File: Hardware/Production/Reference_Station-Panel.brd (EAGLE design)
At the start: 152.4 x 101.6 mm, 395 parts, among them J10 ANTENNA-SMA-GROUNDEDEDGE_SMA, J11 Vertical Qwiic Connector, J2 ANTENNA-SMA-GROUNDEDEDGE_SMA, J3 MICRO-SD-PUSH-PUSH-EXT-PIN, J4 Vertical Qwiic Connector, J7 ANTENNA-SMA-GROUNDEDEDGE_RPSMA, J9 MAGJACK-POE, U1 ESP-WROOM-32E, U10 POE_PSU-DP990X, U11 OPA344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

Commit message: v10 Hardware
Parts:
- removed FRAME1: FRAME-LEDGER, SparkFun-Aesthetics:CREATIVE_COMMONS
- removed LOGO1: SPECIAL_INSTRUCTIONS-ORDERING, SparkFun-Aesthetics:ORDERING_INSTRUCTIONS
- removed VPOE7: TEST-POINTPOGO_PTH, SparkFun-Connectors:1X01_NO_SILK
- added C58: 0.1uF, SparkFun-Capacitors:0603
- added DET, GND: TEST-POINTPOGO_PTH, SparkFun-Connectors:1X01_NO_SILK
- added E$1, E$2, E$3, E$4: (no value), SparkFun-Aesthetics:FIDUCIAL-1X2
- added E$5, E$6: (no value), SparkFun-Retired:FIDUCIAL-1.5X3
- added GNSS_RESET: JUMPER-COMBO_2_NO, SparkFun-Jumpers:COMBO-JUMPER_2_NO
- added R64: 10k, SparkFun-Resistors:0603
- added R65: 100k, SparkFun-Resistors:0603
- added U$154: (no value), output:#GNSS_RESET#0
- added U$155, U$156: (no value), output:DET0
- C31: value DNP -> 0.1uF; device SparkFun-Capacitors:0603_NO_CREAM -> SparkFun-Capacitors:0603
- U$70: device output:CORS_AND_TIME0 -> output:#GNSS_#RESET##0
- U$74: device output:CORS_AND_TIME0 -> output:#RESET#0
- U8: value ADC8045 -> MCP6021T; device SparkFun-IC-Amplifiers:SO08_PAD -> SparkFun-IC-Amplifiers:SOT23-5
- U9: value 74HC4066_QUAD_BILATERAL_SWITCH_QFN -> 74LVC4066D_QUAD_BILATERAL_SWITCH; device SparkFun-IC-Logic:14-QFN -> SparkFun-IC-Logic:SO14
- moved U$74 48.4 mm to (112.7, 61.0), flipped to the top
- moved U$70 35.6 mm to (117.8, 62.9), flipped to the bottom
- moved U$22 10.5 mm to (112.1, 99.4)
- moved U$21 10.5 mm to (89.9, 101.1)
- moved C23 9.93 mm to (120.3, 86.7), turned to 270 degrees
- moved C22 8.98 mm to (120.3, 91.1), turned to 90 degrees
- moved U$41 5.44 mm to (147.5, 61.0)
- moved C26 3.20 mm to (37.1, 32.4)
- moved U9 3.02 mm to (35.2, 26.7), turned to 270 degrees
- moved U$152 2.56 mm to (129.2, 22.9)
- moved U$75 2.56 mm to (75.9, 29.2)
- moved U$153 2.56 mm to (75.9, 22.9)
- moved U$73 2.56 mm to (129.2, 29.2)
- moved R23 2.54 mm to (115.6, 85.1), turned to 0 degrees
- moved R44 2.54 mm to (114.4, 82.5)
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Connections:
- removed net N$16: R9.2, U8.6
- new net DET: DET.1, J3.9, R65.1, U1.4
- new net GNSS_!RESET!: C58.1, GNSS_RESET.1, GNSS_RESET.3, R64.1, U4.49
- net !RESET!: now also GNSS_RESET.2, GNSS_RESET.4; no longer U4.49
- net 3.3V: now also R64.2
- net 3.3V_SW: now also R65.2
- net 5V: now also U8.5; no longer U8.7
- net GND: now also C58.2, GND.1, U8.2; no longer U8.4, U8.PAD, U9.EPAD, VPOE7.1
- net N$18: now also U8.4; no longer U8.2
- net N$26: now also R9.2
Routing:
- net DET: track 0.00 -> 118.1 mm, vias 0 -> 4
- net GNSS_!RESET!: track 0.00 -> 35.8 mm, vias 0 -> 1
- net !RESET!: track 256.6 -> 226.9 mm, vias 9 -> 8
- net ESP25/TP: track 101.6 -> 113.9 mm
- net N$26: track 7.10 -> 13.9 mm, vias 1 -> 2
- net 5V: track 225.2 -> 219.4 mm, vias 43 -> 45
- net ESP2/DAT0: track 89.6 -> 94.2 mm
- net SD_CMD: track 17.4 -> 21.2 mm
- net SD_DAT2: track 23.4 -> 27.0 mm
- net PWREN: track 89.6 -> 93.1 mm, vias 4 -> 2
- net 3.3V_SW: track 348.0 -> 351.3 mm
- net N$16: track 2.96 -> 0.00 mm
- net ESP15/CMD: track 88.8 -> 91.3 mm
- net SD_DAT0: track 25.5 -> 27.8 mm
- net N$29: track 3.71 -> 5.49 mm
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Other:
- board size 152.4 x 101.6 mm -> 165.5 x 131.1 mm
- board text added: "Route Out"
- board text added: "v-score"
- board text added: "v10"
- board text removed: "4-Layers 1.6mm Thickness 1oz Copper Lead-Free HASL Finish Red Solder Resist White Silkscreen"
- board text removed: "Dimensions In Inches"
- board text removed: "Paul Clark"
- board text removed: "v01"

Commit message: Improve TP output at 5V
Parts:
- added R66: 100k, SparkFun-Resistors:0603
- moved Y1 3.56 mm to (62.2, 76.1)
- moved C27 2.69 mm to (66.9, 77.1)
- moved C28 2.69 mm to (66.9, 75.3)
- moved R44 1.63 mm to (115.4, 81.3)
- moved R24 1.52 mm to (64.3, 76.2)
- moved R23 1.37 mm to (116.1, 83.8)
- moved U$71 1.30 mm to (115.4, 82.2)
- moved V_TP 1.30 mm to (115.4, 81.3)
- moved R18 1.28 mm to (117.0, 81.3)
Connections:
- net N$18: now also R66.2
- net N$26: now also R66.1
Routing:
- net N$26: track 13.9 -> 18.1 mm
- net N$20: track 12.2 -> 8.16 mm
- net ESP25/TP: track 113.9 -> 117.5 mm
- net N$19: track 11.6 -> 8.96 mm
- net ESP22/SCL: track 171.6 -> 170.0 mm
- net ESP21/SDA: track 180.3 -> 179.0 mm
- net GND: vias 327 -> 326

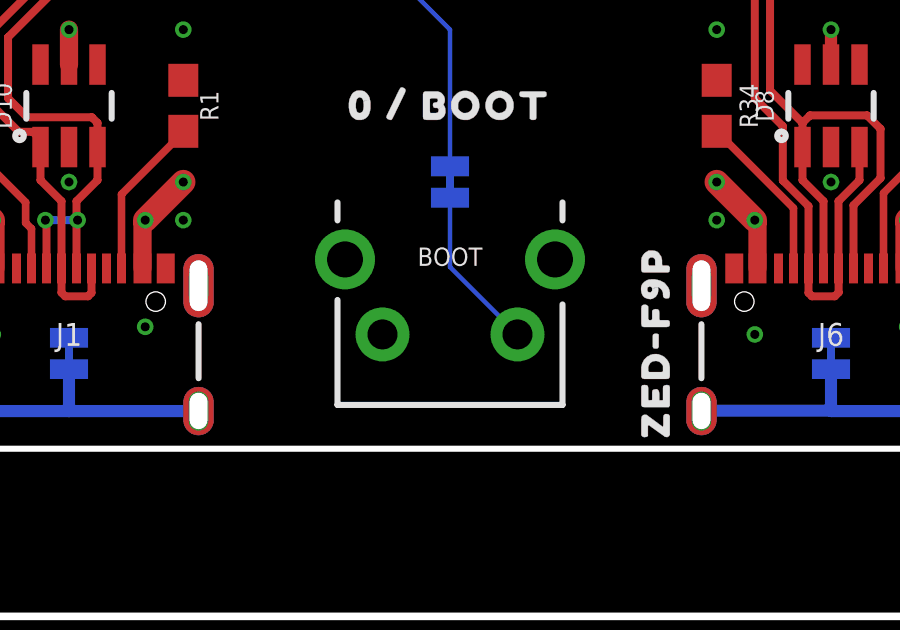
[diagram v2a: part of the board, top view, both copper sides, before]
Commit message: Move BOOT / MODE button further out. Update panels and stickers
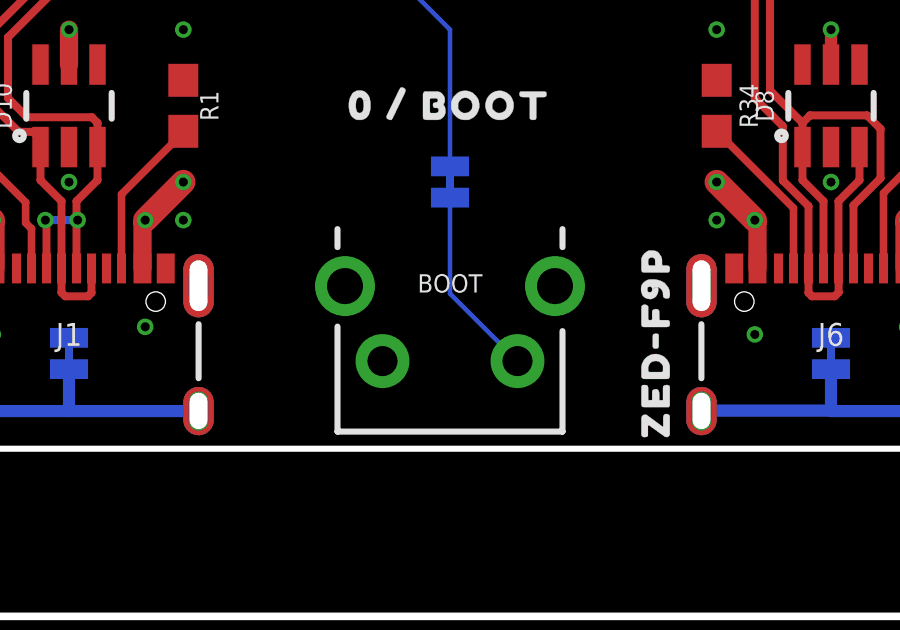
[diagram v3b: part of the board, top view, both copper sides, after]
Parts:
- moved BOOT 0.89 mm to (126.7, 2.92)
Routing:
- net N$29: track 5.49 -> 6.38 mm
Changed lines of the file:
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@@
 <layers>
 <layer number="1" name="Top" color="4" fill="1" visible="yes" active="yes"/>
-<layer number="2" name="Route2" color="16" fill="1" visible="no" active="yes"/>
+<layer number="2" name="Route2" color="63" fill="1" visible="no" active="yes"/>
 <layer number="3" name="Route3" color="17" fill="1" visible="no" active="no"/>
 <layer number="4" name="Route4" color="18" fill="1" visible="no" active="no"/>
@@
 <layer number="19" name="Unrouted" color="6" fill="1" visible="yes" active="yes"/>
 <layer number="20" name="Dimension" color="24" fill="1" visible="yes" active="yes"/>
-<layer number="21" name="tPlace" color="7" fill="1" visible="yes" active="yes"/>
-<layer number="22" name="bPlace" color="7" fill="1" visible="yes" active="yes"/>
+<layer number="21" name="tPlace" color="16" fill="1" visible="yes" active="yes"/>
+<layer number="22" name="bPlace" color="14" fill="1" visible="yes" active="yes"/>
 <layer number="23" name="tOrigins" color="15" fill="1" visible="yes" active="yes"/>
 <layer number="24" name="bOrigins" color="15" fill="1" visible="yes" active="yes"/>
-<layer number="25" name="tNames" color="7" fill="1" visible="yes" active="yes"/>
-<layer number="26" name="bNames" color="7" fill="1" visible="yes" active="yes"/>
-<layer number="27" name="tValues" color="7" fill="1" visible="yes" active="yes"/>
-<layer number="28" name="bValues" color="7" fill="1" visible="yes" active="yes"/>
-<layer number="29" name="tStop" color="7" fill="3" visible="yes" active="yes"/>
-<layer number="30" name="bStop" color="7" fill="6" visible="yes" active="yes"/>
-<layer number="31" name="tCream" color="7" fill="4" visible="yes" active="yes"/>
-<layer number="32" name="bCream" color="7" fill="5" visible="yes" active="yes"/>
-<layer number="33" name="tFinish" color="6" fill="3" visible="yes" active="yes"/>
-<layer number="34" name="bFinish" color="6" fill="6" visible="yes" active="yes"/>
-<layer number="35" name="tGlue" color="7" fill="4" visible="yes" active="yes"/>
-<layer number="36" name="bGlue" color="7" fill="5" visible="yes" active="yes"/>
-<layer number="37" name="tTest" color="7" fill="1" visible="yes" active="yes"/>
-<layer number="38" name="bTest" color="7" fill="1" visible="yes" active="yes"/>
-<layer number="39" name="tKeepout" color="4" fill="11" visible="yes" active="yes"/>
-<layer number="40" name="bKeepout" color="1" fill="11" visible="yes" active="yes"/>
-<layer number="41" name="tRestrict" color="4" fill="10" visible="yes" active="yes"/>
-<layer number="42" name="bRestrict" color="1" fill="10" visible="yes" active="yes"/>
-<layer number="43" name="vRestrict" color="2" fill="10" visible="yes" active="yes"/>
-<layer number="44" name="Drills" color="7" fill="1" visible="yes" active="yes"/>
+<layer number="25" name="tNames" color="7" fill="1" visible="no" active="yes"/>
+<layer number="26" name="bNames" color="7" fill="1" visible="no" active="yes"/>
+<layer number="27" name="tValues" color="7" fill="1" visible="no" active="yes"/>
+<layer number="28" name="bValues" color="7" fill="1" visible="no" active="yes"/>
+<layer number="29" name="tStop" color="7" fill="3" visible="no" active="yes"/>
+<layer number="30" name="bStop" color="7" fill="6" visible="no" active="yes"/>
+<layer number="31" name="tCream" color="7" fill="4" visible="no" active="yes"/>
+<layer number="32" name="bCream" color="7" fill="5" visible="no" active="yes"/>
+<layer number="33" name="tFinish" color="6" fill="3" visible="no" active="yes"/>
+<layer number="34" name="bFinish" color="6" fill="6" visible="no" active="yes"/>
+<layer number="35" name="tGlue" color="7" fill="4" visible="no" active="yes"/>
+<layer number="36" name="bGlue" color="7" fill="5" visible="no" active="yes"/>
+<layer number="37" name="tTest" color="7" fill="1" visible="no" active="yes"/>
+<layer number="38" name="bTest" color="7" fill="1" visible="no" active="yes"/>
+<layer number="39" name="tKeepout" color="4" fill="11" visible="no" active="yes"/>
+<layer number="40" name="bKeepout" color="1" fill="11" visible="no" active="yes"/>
+<layer number="41" name="tRestrict" color="4" fill="10" visible="no" active="yes"/>
+<layer number="42" name="bRestrict" color="1" fill="10" visible="no" active="yes"/>
+<layer number="43" name="vRestrict" color="2" fill="10" visible="no" active="yes"/>
+<layer number="44" name="Drills" color="7" fill="1" visible="no" active="yes"/>
 <layer number="45" name="Holes" color="7" fill="1" visible="yes" active="yes"/>
-<layer number="46" name="Milling" color="3" fill="1" visible="yes" active="yes"/>
-<layer number="47" name="Measures" color="7" fill="1" visible="yes" active="yes"/>
-<layer number="48" name="Document" color="7" fill="1" visible="yes" active="yes"/>
-<layer number="49" name="Reference" color="7" fill="1" visible="yes" active="yes"/>
-<layer number="50" name="dxf" color="7" fill="1" visible="yes" active="yes"/>
-<layer number="51" name="tDocu" color="7" fill="1" visible="yes" active="yes"/>
-<layer number="52" name="bDocu" color="7" fill="1" visible="yes" active="yes"/>
+<layer number="46" name="Milling" color="3" fill="1" visible="no" active="yes"/>
+<layer number="47" name="Measures" color="7" fill="1" visible="no" active="yes"/>
+<layer number="48" name="Document" color="7" fill="1" visible="no" active="yes"/>
+<layer number="49" name="Reference" color="7" fill="1" visible="no" active="yes"/>
+<layer number="50" name="dxf" color="7" fill="1" visible="no" active="yes"/>
+<layer number="51" name="tDocu" color="6" fill="1" visible="yes" active="yes"/>
+<layer number="52" name="bDocu" color="7" fill="1" visible="no" active="yes"/>
 <layer number="53" name="tGND_GNDA" color="7" fill="9" visible="no" active="no"/>
 <layer number="54" name="bGND_GNDA" color="1" fill="9" visible="no" active="no"/>
@@
 <attribute name="PROD_ID" value="SWCH-13896" x="101.2825" y="3.81" size="1.778" layer="27" ratio="15" display="off"/>
 </element>
-<element name="BOOT" library="SparkFun-Switches" package="TACTILE_SWITCH_PTH_RA_8-020" value="MOMENTARY-SWITCH-SPST-PTH-RIGHT-ANGLE-8-020" x="126.6825" y="3.81" smashed="yes">
-<attribute name="NAME" x="126.6825" y="6.096" size="0.6096" layer="25" font="vector" ratio="20" align="bottom-center"/>
-<attribute name="PROD_ID" value="SWCH-13896" x="126.6825" y="3.81" size="1.778" layer="27" ratio="15" display="off"/>
+<element name="BOOT" library="SparkFun-Switches" package="TACTILE_SWITCH_PTH_RA_8-020" value="MOMENTARY-SWITCH-SPST-PTH-RIGHT-ANGLE-8-020" x="126.6825" y="2.921" smashed="yes">
+<attribute name="NAME" x="126.6825" y="5.207" size="0.6096" layer="25" font="vector" ratio="20" align="bottom-center"/>
+<attribute name="PROD_ID" value="SWCH-13896" x="126.6825" y="2.921" size="1.778" layer="27" ratio="15" display="off"/>
 </element>
 <element name="LED" library="SparkFun-Jumpers" package="SMT-JUMPER_2_NC_TRACE_SILK" package3d_urn="urn:adsk.eagle:package:39281/1" value="JUMPER-SMT_2_NC_TRACE_SILK" x="12.3825" y="3.175" smashed="yes" rot="MR180">
@@
 <wire x1="117.0305" y1="79.248" x2="117.0305" y2="80.43" width="0" layer="19" extent="1-1"/>
 <wire x1="116.9425" y1="64.135" x2="125.9365" y2="63.57" width="0" layer="19" extent="1-1"/>
-<wire x1="124.4325" y1="3.81" x2="135.5725" y2="7.62" width="0" layer="19" extent="1-1"/>
-<wire x1="117.2075" y1="6.01" x2="124.4325" y2="3.81" width="0" layer="19" extent="1-1"/>
+<wire x1="124.4325" y1="2.921" x2="135.5725" y2="7.62" width="0" layer="19" extent="1-1"/>
+<wire x1="117.2075" y1="6.01" x2="124.4325" y2="2.921" width="0" layer="19" extent="1-1"/>
 <wire x1="117.7925" y1="7.62" x2="117.2075" y2="6.01" width="0" layer="19" extent="1-1"/>
 <wire x1="116.5225" y1="4.064" x2="117.2075" y2="6.01" width="0" layer="19" extent="1-1"/>
@@
 <contactref element="BOOT" pad="2"/>
 <contactref element="BOOT_SW" pad="2"/>
-<wire x1="128.9325" y1="3.81" x2="126.6825" y2="6.06" width="0.1524" layer="16"/>
-<wire x1="126.6825" y1="6.06" x2="126.6825" y2="8.3693" width="0.1524" layer="16"/>
+<wire x1="126.6825" y1="5.171" x2="128.9325" y2="2.921" width="0.1524" layer="16"/>
+<wire x1="126.6825" y1="8.3693" x2="126.6825" y2="5.171" width="0.1524" layer="16"/>
 </signal>
 <signal name="GNSS_!RESET!">

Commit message: Replace OPA344 with MCP6021T-E/OT
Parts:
- U11, U13: value OPA344 -> MCP6021T
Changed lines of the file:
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@@
 <attribute name="VALUE" x="119.0625" y="54.102" size="0.6096" layer="27" font="vector" ratio="20" rot="R180" align="top-center"/>
 </element>
-<element name="U11" library="SparkFun-IC-Amplifiers" package="SOT23-5" value="OPA344" x="128.5875" y="78.74" smashed="yes" rot="R90">
+<element name="U11" library="SparkFun-IC-Amplifiers" package="SOT23-5" value="MCP6021T" x="128.5875" y="78.74" smashed="yes" rot="R90">
 <attribute name="NAME" x="128.5875" y="76.835" size="0.6096" layer="25" font="vector" ratio="20" rot="R180" align="bottom-center"/>
-<attribute name="PROD_ID" value="IC-08251" x="124.7775" y="74.93" size="1.778" layer="27" ratio="15" rot="R90" display="off"/>
+<attribute name="PROD_ID" value="IC-12504" x="124.7775" y="74.93" size="1.778" layer="27" ratio="15" rot="R90" display="off"/>
 <attribute name="VALUE" x="128.5875" y="81.28" size="0.6096" layer="27" font="vector" ratio="20" rot="R180" align="bottom-center"/>
 </element>
@@
 <attribute name="VALUE" x="133.1595" y="78.74" size="0.6096" layer="27" font="vector" ratio="20" rot="R90" align="top-center"/>
 </element>
-<element name="U13" library="SparkFun-IC-Amplifiers" package="SOT23-5" value="OPA344" x="128.5875" y="74.93" smashed="yes" rot="R90">
+<element name="U13" library="SparkFun-IC-Amplifiers" package="SOT23-5" value="MCP6021T" x="128.5875" y="74.93" smashed="yes" rot="R90">
 <attribute name="NAME" x="128.5875" y="73.025" size="0.6096" layer="25" font="vector" ratio="20" rot="R180" align="bottom-center"/>
-<attribute name="PROD_ID" value="IC-08251" x="128.5875" y="74.93" size="1.778" layer="27" ratio="15" rot="R90" display="off"/>
+<attribute name="PROD_ID" value="IC-12504" x="128.5875" y="74.93" size="1.778" layer="27" ratio="15" rot="R90" display="off"/>
 <attribute name="VALUE" x="128.5875" y="77.47" size="0.6096" layer="27" font="vector" ratio="20" rot="R180" align="bottom-center"/>
 </element>

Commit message: Change LED to GREEN
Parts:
- D2: value LED-RIGHT-ANGLE-PTH-BLUE -> LED-RIGHT-ANGLE-PTH-GREEN
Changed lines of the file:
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@@
 <attribute name="NAME" x="12.3825" y="2.032" size="0.6096" layer="26" font="vector" ratio="20" rot="MR180" align="bottom-center"/>
 </element>
-<element name="D2" library="SparkFun-LED" package="CBI-RIGHT-ANGLE-PTH" value="LED-RIGHT-ANGLE-PTH-BLUE" x="12.3825" y="0.635" smashed="yes">
+<element name="D2" library="SparkFun-LED" package="CBI-RIGHT-ANGLE-PTH" value="LED-RIGHT-ANGLE-PTH-GREEN" x="12.3825" y="0.635" smashed="yes">
 <attribute name="NAME" x="12.3825" y="10.795" size="1.27" layer="25" font="vector" rot="SR0" align="bottom-center"/>
-<attribute name="PROD_ID" value="DIO-13890" x="12.3825" y="0.635" size="1.778" layer="27" ratio="15" display="off"/>
+<attribute name="PROD_ID" value="DIO-13847" x="12.3825" y="0.635" size="1.778" layer="27" ratio="15" display="off"/>
 </element>
 <element name="R62" library="SparkFun-Resistors" package="0603" value="470" x="75.8825" y="67.31" smashed="yes" rot="R180">
